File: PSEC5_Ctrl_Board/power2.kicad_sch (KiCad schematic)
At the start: 75 parts, among them J7 1766343, J8 1766343, J9 1766343, U13 SIC473ED-T1-GE3, U15 OKX-T/5-D12N-C, U16 OKX-T/5-D12N-C

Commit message: Added comments
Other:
- note added: "2V5 External Buck"
- note added: "5V0 External Buck"
- moved on the sheet: J8, R25, U15
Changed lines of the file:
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@@
 	)
 	(junction
-		(at 210.82 189.23)
+		(at 212.09 179.07)
 		(diameter 0)
 		(color 0 0 0 0)
@@
 	)
 	(junction
-		(at 264.16 205.74)
+		(at 265.43 195.58)
 		(diameter 0)
 		(color 0 0 0 0)
@@
 	)
 	(no_connect
-		(at 208.28 191.77)
+		(at 209.55 181.61)
 	)
 	(no_connect
-		(at 233.68 191.77)
+		(at 234.95 181.61)
 	)
 	(no_connect
@@
 	(wire
 		(pts
-			(xy 264.16 205.74) (xy 264.16 208.28)
+			(xy 265.43 195.58) (xy 265.43 198.12)
 		)
 		(stroke
@@
 	(wire
 		(pts
-			(xy 299.72 205.74) (xy 299.72 203.2)
+			(xy 300.99 195.58) (xy 300.99 193.04)
 		)
 		(stroke
@@
 	(wire
 		(pts
-			(xy 227.33 205.74) (xy 264.16 205.74)
+			(xy 228.6 195.58) (xy 265.43 195.58)
 		)
 		(stroke
@@
 	(wire
 		(pts
-			(xy 264.16 205.74) (xy 299.72 205.74)
+			(xy 265.43 195.58) (xy 300.99 195.58)
 		)
 		(stroke
@@
 	(wire
 		(pts
-			(xy 294.64 191.77) (xy 318.77 191.77)
+			(xy 295.91 181.61) (xy 320.04 181.61)
 		)
 		(stroke
@@
 	(wire
 		(pts
-			(xy 299.72 189.23) (xy 299.72 198.12)
+			(xy 300.99 179.07) (xy 300.99 187.96)
 		)
 		(stroke
@@
 	(wire
 		(pts
-			(xy 210.82 189.23) (xy 233.68 189.23)
+			(xy 212.09 179.07) (xy 234.95 179.07)
 		)
 		(stroke
@@
 	(wire
 		(pts
-			(xy 233.68 186.69) (xy 227.33 186.69)
+			(xy 234.95 176.53) (xy 228.6 176.53)
 		)
 		(stroke
@@
 	(wire
 		(pts
-			(xy 294.64 189.23) (xy 299.72 189.23)
+			(xy 295.91 179.07) (xy 300.99 179.07)
 		)
 		(stroke
@@
 	(wire
 		(pts
-			(xy 227.33 186.69) (xy 227.33 205.74)
+			(xy 228.6 176.53) (xy 228.6 195.58)
 		)
 		(stroke
@@
 	(wire
 		(pts
-			(xy 208.28 189.23) (xy 210.82 189.23)
+			(xy 209.55 179.07) (xy 212.09 179.07)
 		)
 		(stroke
@@
 		)
 	)
+	(text "2V5 External Buck"
+		(exclude_from_sim no)
+		(at 266.7 211.074 0)
+		(effects
+			(font
+				(size 3 3)
+			)
+		)
+	)
 	(text "Vmin = 3.19V\nVtyp = 3.30V\nVmax = 3.435V"
 		(exclude_from_sim no)
@@
 		)
 	)
+	(text "5V0 External Buck"
+		(exclude_from_sim no)
+		(at 260.858 151.384 0)
+		(effects
+			(font
+				(size 3 3)
+			)
+		)
+	)
 	(text "Physical Connector (Plug)\n6V-55V"
 		(exclude_from_sim no)
@@
 	(global_label "VDD_BUCK_5V"
 		(shape output)
-		(at 318.77 191.77 0)
+		(at 320.04 181.61 0)
 		(fields_autoplaced yes)
 		(effects
@@
 		)
 		(property "Intersheetrefs" "${INTERSHEET_REFS}"
-			(at 334.7576 191.77 0)
+			(at 336.0276 181.61 0)
 			(effects
 				(font
@@
 	(symbol
 		(lib_id "power:PWR_FLAG")
-		(at 210.82 189.23 0)
+		(at 212.09 179.07 0)
 		(unit 1)
 		(exclude_from_sim no)
@@
 		(fields_autoplaced yes)
 		(property "Reference" "#FLG027"
-			(at 210.82 187.325 0)
+			(at 212.09 177.165 0)
 			(effects
 				(font
@@
 		)
 		(property "Value" "PWR_FLAG"
-			(at 210.82 184.15 0)
+			(at 212.09 173.99 0)
 			(effects
 				(font
@@
 		)
 		(property "Footprint" ""
-			(at 210.82 189.23 0)
+			(at 212.09 179.07 0)
 			(effects
 				(font
@@
 		)
 		(property "Datasheet" "~"
-			(at 210.82 189.23 0)
+			(at 212.09 179.07 0)
 			(effects
 				(font
@@
 		)
 		(property "Description" "Special symbol for telling ERC where power comes from"
-			(at 210.82 189.23 0)
+			(at 212.09 179.07 0)
 			(effects
 				(font
@@
 	(symbol
 		(lib_id "power:GND")
-		(at 264.16 208.28 0)
+		(at 265.43 198.12 0)
 		(unit 1)
 		(exclude_from_sim no)
@@
 		(fields_autoplaced yes)
 		(property "Reference" "#PWR026"
-			(at 264.16 214.63 0)
+			(at 265.43 204.47 0)
 			(effects
 				(font
@@
 		)
 		(property "Value" "GND"
-			(at 264.16 213.36 0)
+			(at 265.43 203.2 0)
 			(effects
 				(font
@@
 		)
 		(property "Footprint" ""
-			(at 264.16 208.28 0)
+			(at 265.43 198.12 0)
 			(effects
 				(font
@@
 		)
 		(property "Datasheet" ""
-			(at 264.16 208.28 0)
+			(at 265.43 198.12 0)
 			(effects
 				(font
@@
 		)
 		(property "Description" "Power symbol creates a global label with name \"GND\" , ground"
-			(at 264.16 208.28 0)
+			(at 265.43 198.12 0)
 			(effects
 				(font
@@
 	(symbol
 		(lib_id "PSEC5_ctrlbd:OKX-T_5-D12N-C")
-		(at 294.64 191.77 180)
+		(at 295.91 181.61 180)
 		(unit 1)
 		(exclude_from_sim no)
@@
 		(fields_autoplaced yes)
 		(property "Reference" "U15"
-			(at 264.16 176.53 0)
+			(at 265.43 166.37 0)
 			(effects
 				(font
@@
 		)
 		(property "Value" "OKX-T/5-D12N-C"
-			(at 264.16 179.07 0)
+			(at 265.43 168.91 0)
 			(effects
 				(font
@@
 		)
 		(property "Footprint" "OKX-T/5-D12N-C_MUR"
-			(at 278.13 211.328 0)
+			(at 279.4 201.168 0)
 			(effects
 				(font
@@
 		)
 		(property "Datasheet" "OKX-T/5-D12N-C"
-			(at 279.654 207.772 0)
+			(at 280.924 197.612 0)
 			(effects
 				(font
@@
 		)
 		(property "Description" ""
-			(at 294.64 191.77 0)
+			(at 295.91 181.61 0)
 			(effects
 				(font
@@
 	(symbol
 		(lib_id "Device:R_Small_US")
-		(at 299.72 200.66 180)
+		(at 300.99 190.5 180)
 		(unit 1)
 		(exclude_from_sim no)
@@
 		(dnp no)
 		(property "Reference" "R25"
-			(at 297.18 200.406 90)
+			(at 298.45 190.246 90)
 			(effects
 				(font
@@
 		)
 		(property "Value" "1.472k"
-			(at 302.768 199.39 90)
+			(at 304.038 189.23 90)
 			(effects
 				(font
@@
 		)
 		(property "Footprint" "Resistor_SMD:R_0603_1608Metric"
-			(at 299.72 200.66 0)
+			(at 300.99 190.5 0)
 			(effects
 				(font
@@
 		)
 		(property "Datasheet" "~"
-			(at 299.72 200.66 0)
+			(at 300.99 190.5 0)
 			(effects
 				(font
@@
 		)
 		(property "Description" "Resistor, small US symbol"
-			(at 299.72 200.66 0)
+			(at 300.99 190.5 0)
 			(effects
 				(font
@@
 	(symbol
 		(lib_id "PSEC5_ctrlbd:1766343")
-		(at 208.28 189.23 0)
+		(at 209.55 179.07 0)
 		(mirror y)
 		(unit 1)
@@
 		(dnp no)
 		(property "Reference" "J8"
-			(at 194.31 189.2299 0)
+			(at 195.58 179.0699 0)
 			(effects
 				(font
@@
 		)
 		(property "Value" "1766343"
-			(at 194.31 191.7699 0)
+			(at 195.58 181.6099 0)
 			(effects
 				(font
@@
 		)
 		(property "Footprint" "Connector_Phoenix_GMSTB:PhoenixContact_GMSTBA_2,5_2-G_1x02_P7.50mm_Horizontal"
-			(at 200.66 179.832 0)
+			(at 201.93 169.672 0)
 			(effects
 				(font
@@
 		)
 		(property "Datasheet" "1766343"
-			(at 202.946 177.8 0)
+			(at 204.216 167.64 0)
 			(effects
 				(font
@@
 		)
 		(property "Description" ""
-			(at 208.28 189.23 0)
+			(at 209.55 179.07 0)
 			(effects
 				(font

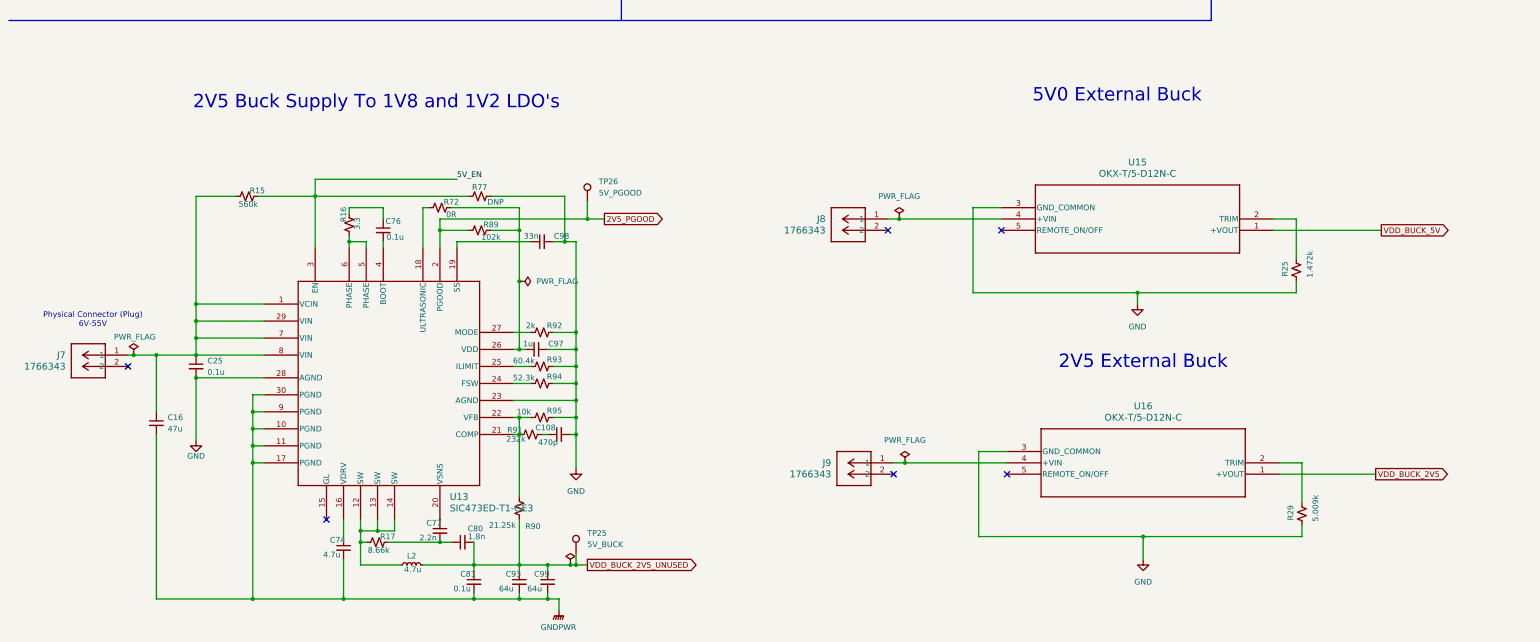
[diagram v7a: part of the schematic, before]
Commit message: rearranged samtec
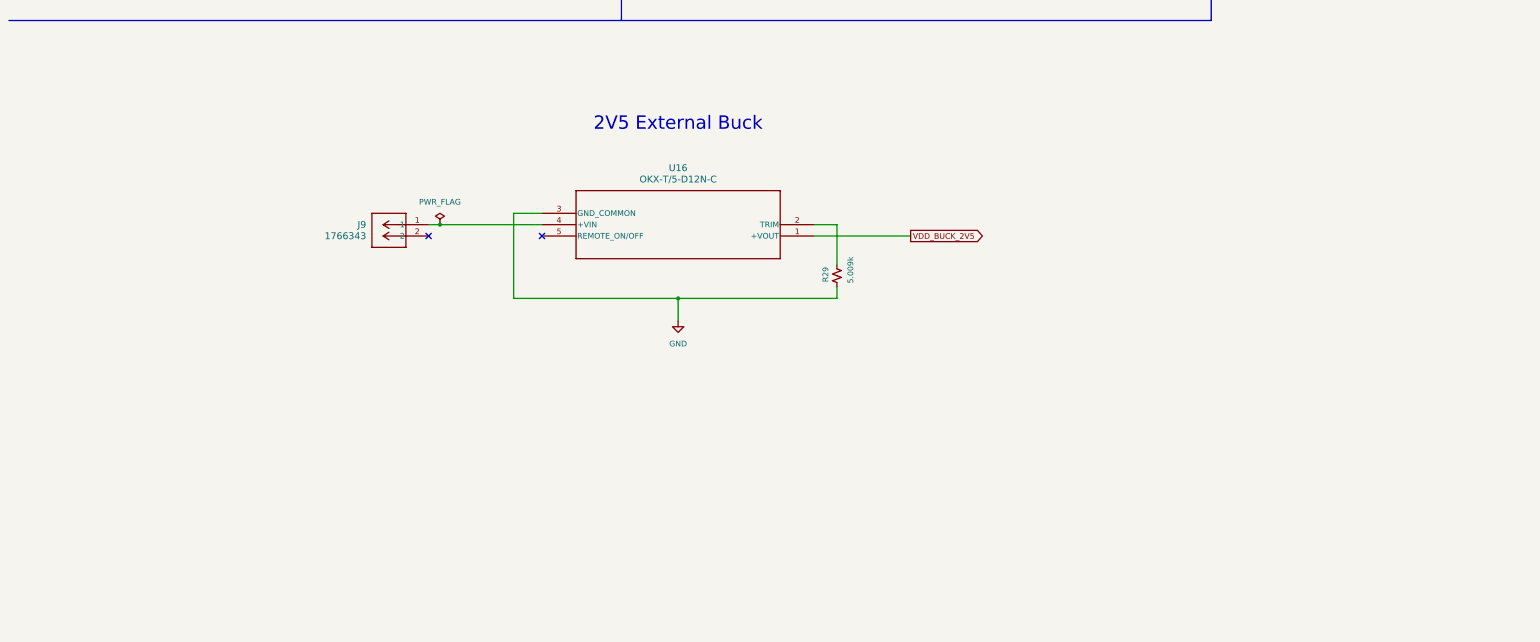
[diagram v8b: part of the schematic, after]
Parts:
- removed C108: 470p, Capacitor_SMD:C_0603_1608Metric, symbol Device:C_Small
- removed C16: 47u, Capacitor_SMD:C_0603_1608Metric, symbol Device:C_Small
- removed C25, C76, C81: 0.1u, Capacitor_SMD:C_0603_1608Metric, symbol Device:C_Small
- removed C74: 4.7u, Capacitor_SMD:C_0603_1608Metric, symbol Device:C_Small
- removed C77: 2.2n, Capacitor_SMD:C_0603_1608Metric, symbol Device:C_Small
- removed C80: 1.8n, Capacitor_SMD:C_0603_1608Metric, symbol Device:C_Small
- removed C93, C99: 64u, Capacitor_SMD:C_0603_1608Metric, symbol Device:C_Small
- removed C97: 1u, Capacitor_SMD:C_0603_1608Metric, symbol Device:C_Small
- removed C98: 33n, Capacitor_SMD:C_0603_1608Metric, symbol Device:C_Small
- removed J7, J8: 1766343, Connector_Phoenix_GMSTB:PhoenixContact_GMSTBA_2,5_2-G_1x02_P7.50mm_Horizontal, symbol PSEC5_ctrlbd:1766343
- removed L2: 4.7u, symbol Device:L_Small
- removed R15: 560k, Resistor_SMD:R_0603_1608Metric, symbol Device:R_Small_US
- removed R16: 3.3, Resistor_SMD:R_0603_1608Metric, symbol Device:R_Small_US
- removed R17: 8.66k, Resistor_SMD:R_0603_1608Metric, symbol Device:R_Small_US
- removed R25: 1.472k, Resistor_SMD:R_0603_1608Metric, symbol Device:R_Small_US
- removed R72: 0R, Resistor_SMD:R_0603_1608Metric, symbol Device:R_Small_US
- removed R77: DNP, Resistor_SMD:R_0603_1608Metric, symbol Device:R_Small_US
- removed R89: 102k, Resistor_SMD:R_0603_1608Metric, symbol Device:R_Small_US
- removed R90: 21.25k, Resistor_SMD:R_0603_1608Metric, symbol Device:R_Small_US
- removed R91: 232k, Resistor_SMD:R_0603_1608Metric, symbol Device:R_Small_US
- removed R92: 2k, Resistor_SMD:R_0603_1608Metric, symbol Device:R_Small_US
- removed R93: 60.4k, Resistor_SMD:R_0603_1608Metric, symbol Device:R_Small_US
- removed R94: 52.3k, Resistor_SMD:R_0603_1608Metric, symbol Device:R_Small_US
- removed R95: 10k, Resistor_SMD:R_0603_1608Metric, symbol Device:R_Small_US
- removed TP25: 5V_BUCK, TestPoint:TestPoint_Bridge_Pitch2.0mm_Drill0.7mm, symbol Connector:TestPoint
- removed TP26: 5V_PGOOD, TestPoint:TestPoint_Bridge_Pitch2.0mm_Drill0.7mm, symbol Connector:TestPoint
- removed U13: SIC473ED-T1-GE3, PowerPAK_MLP55-27L_VIS, symbol PSEC5_ctrlbd:SIC473ED-T1-GE3
- removed U15: OKX-T/5-D12N-C, OKX-T/5-D12N-C_MUR, symbol PSEC5_ctrlbd:OKX-T_5-D12N-C
- U16: footprint OKX-T/5-D12N-C_MUR -> OKX_T_5_D12N_C:OKX-T&slash_5-D12N-C_MUR
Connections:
- no-connect marks 6 -> 2
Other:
- note removed: "2V5 Buck Supply To 1V8 and 1V2 LDO's"
- note removed: "5V0 External Buck"
- note removed: "Physical Connector (Plug) 6V-55V"
- moved on the sheet: J9, R29, U16
